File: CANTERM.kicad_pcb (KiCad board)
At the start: 2 copper layers, 25.4 x 50.8 mm, 10 parts, among them J1 Conn_01x03_Pin, J2 Conn_01x03_Pin, J3 Conn_01x03_Pin, M1 MountingHole_10, M2 MountingHole_10, SW1 SW_DIP_x01

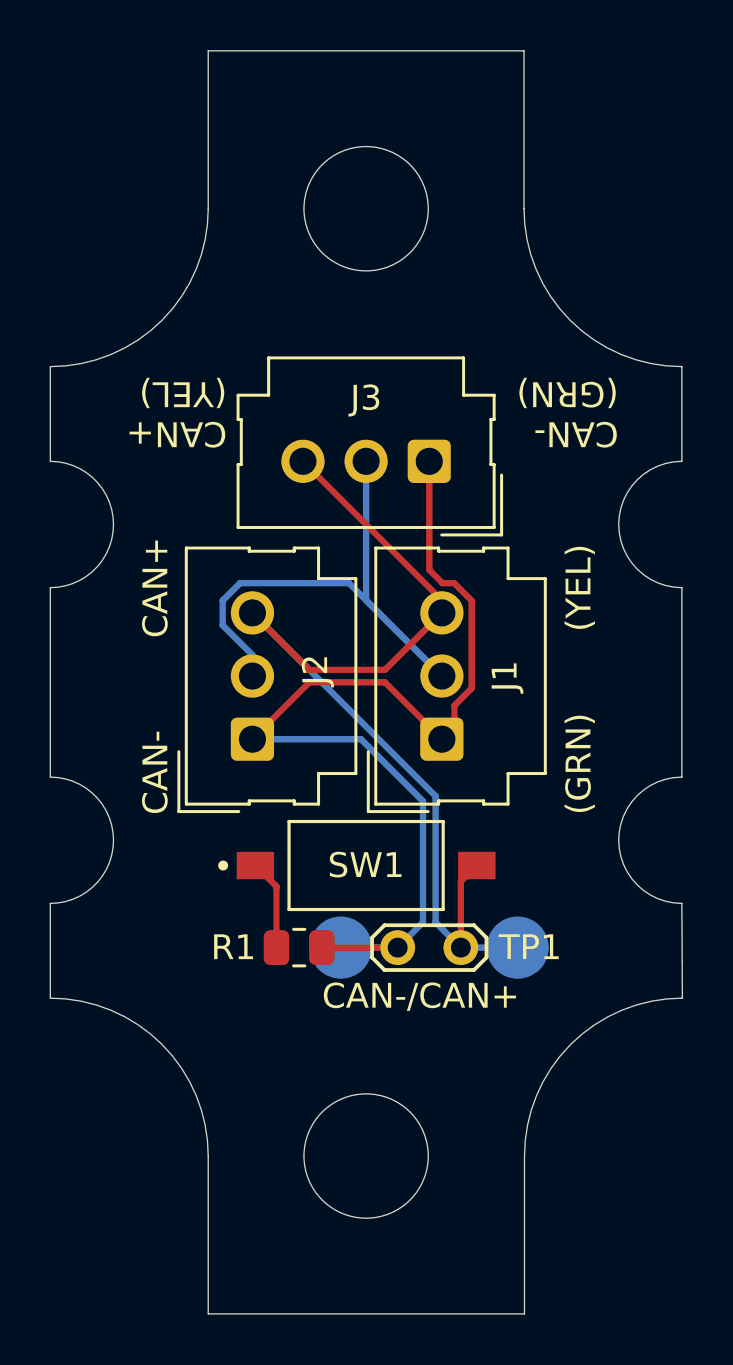
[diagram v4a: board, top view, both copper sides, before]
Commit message: slightly shrink board so it fits _inside_ the space envelope
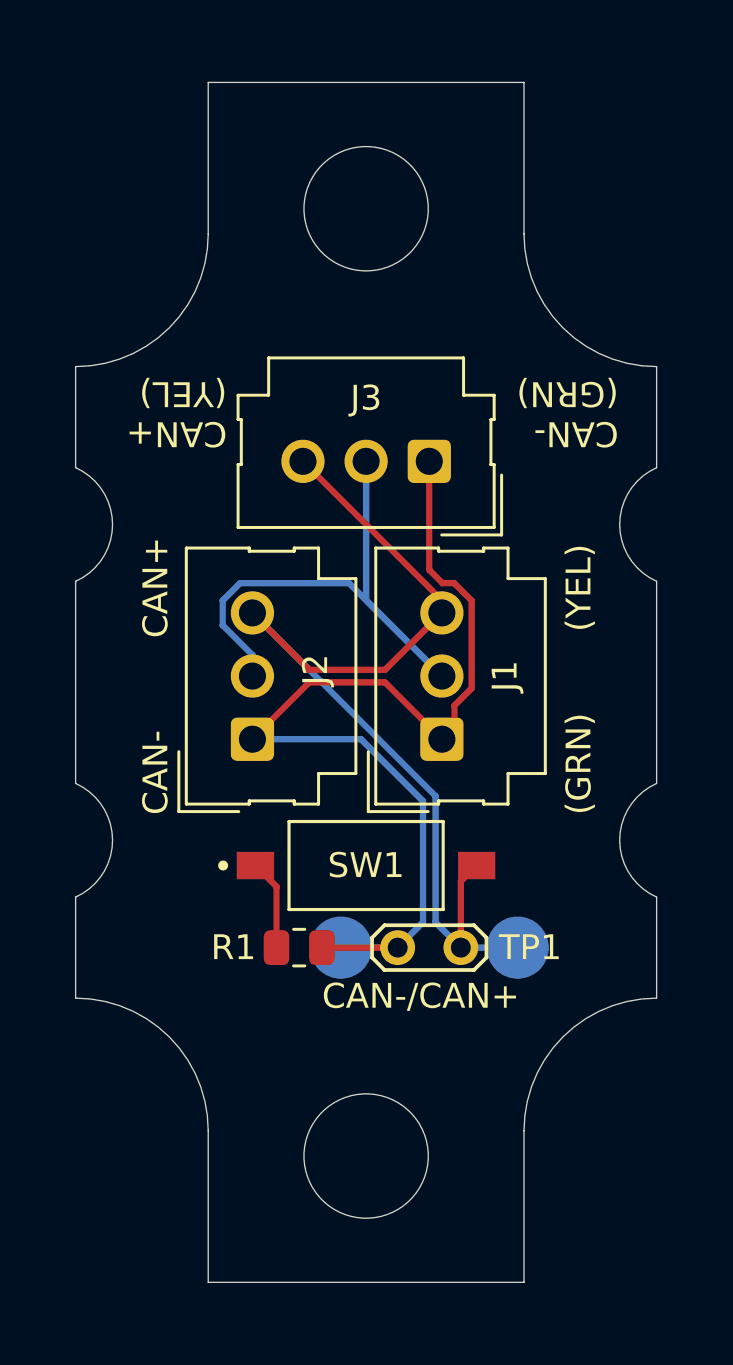
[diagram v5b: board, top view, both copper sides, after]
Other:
- board size 25.4 x 50.8 mm -> 23.4 x 48.3 mm
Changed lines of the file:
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@@
 		)
 	)
-	(gr_line
-		(start 100 60.16)
-		(end 100 56.35)
+	(gr_arc
+		(start 101.016 73.114001)
+		(mid 102.501609 75.4)
+		(end 101.016 77.685999)
 		(stroke
 			(width 0.05)
@@
 	)
 	(gr_arc
-		(start 100 72.86)
-		(mid 102.54 75.4)
-		(end 100 77.94)
-		(locked yes)
+		(start 106.35 51.016)
+		(mid 104.787708 54.787708)
+		(end 101.016 56.35)
 		(stroke
 			(width 0.05)
@@
 	)
 	(gr_line
-		(start 106.35 43.65)
-		(end 106.35 50)
+		(start 124.384 77.686)
+		(end 124.384 81.75)
 		(stroke
 			(width 0.05)
@@
 	)
 	(gr_line
-		(start 125.4 65.24)
-		(end 125.4 72.86)
-		(locked yes)
+		(start 124.384 56.35)
+		(end 124.384 60.414)
+		(stroke
+			(width 0.05)
+			(type default)
+		)
+		(layer "Edge.Cuts")
+	)
+	(gr_line
+		(start 101.016 60.414)
+		(end 101.016 56.35)
 		(stroke
 			(width 0.05)
@@
 	)
 	(gr_arc
-		(start 100 60.16)
-		(mid 102.54 62.7)
-		(end 100 65.24)
-		(locked yes)
+		(start 119.05 87.084)
+		(mid 120.612292 83.312292)
+		(end 124.384 81.75)
 		(stroke
 			(width 0.05)
@@
 	)
 	(gr_arc
-		(start 125.4 56.35)
-		(mid 120.909872 54.490128)
-		(end 119.05 50)
+		(start 124.384 64.985999)
+		(mid 122.898391 62.7)
+		(end 124.384 60.414001)
 		(stroke
 			(width 0.05)
@@
 	)
 	(gr_line
-		(start 125.4 56.35)
-		(end 125.4 60.16)
+		(start 106.35 93.18)
+		(end 119.05 93.18)
+		(stroke
+			(width 0.05)
+			(type default)
+		)
+		(layer "Edge.Cuts")
+	)
+	(gr_line
+		(start 106.35 44.92)
+		(end 106.35 51.016)
+		(stroke
+			(width 0.05)
+			(type default)
+		)
+		(layer "Edge.Cuts")
+	)
+	(gr_line
+		(start 119.05 93.18)
+		(end 119.05 87.084)
 		(stroke
 			(width 0.05)
@@
 	)
 	(gr_arc
-		(start 106.35 50)
-		(mid 104.490128 54.490128)
-		(end 100 56.35)
+		(start 101.016 60.414)
+		(mid 102.501609 62.699999)
+		(end 101.016 64.985998)
 		(stroke
 			(width 0.05)
@@
 	)
 	(gr_arc
-		(start 125.4 77.94)
-		(mid 122.86 75.4)
-		(end 125.4 72.86)
-		(locked yes)
+		(start 101.016 81.75)
+		(mid 104.787708 83.312292)
+		(end 106.35 87.084)
 		(stroke
 			(width 0.05)
@@
 	)
 	(gr_line
-		(start 100 72.86)
-		(end 100 65.24)
-		(locked yes)
+		(start 101.016 73.114)
+		(end 101.016 64.986)
 		(stroke
 			(width 0.05)
@@
 	)
 	(gr_line
-		(start 125.42 81.75)
-		(end 125.4 77.94)
+		(start 101.016 81.75)
+		(end 101.016 77.686)
 		(stroke
 			(width 0.05)
@@
 	)
 	(gr_line
-		(start 100 81.75)
-		(end 100 77.94)
+		(start 106.35 87.084)
+		(end 106.35 93.18)
+		(stroke
+			(width 0.05)
+			(type default)
+		)
+		(layer "Edge.Cuts")
+	)
+	(gr_arc
+		(start 124.384 77.686)
+		(mid 122.898391 75.400001)
+		(end 124.384 73.114002)
 		(stroke
 			(width 0.05)
@@
 	)
 	(gr_line
-		(start 106.35 94.45)
-		(end 106.35 88.1)
+		(start 119.05 44.92)
+		(end 106.35 44.92)
+		(stroke
+			(width 0.05)
+			(type default)
+		)
+		(layer "Edge.Cuts")
+	)
+	(gr_arc
+		(start 124.384 56.35)
+		(mid 120.612292 54.787708)
+		(end 119.05 51.016)
 		(stroke
 			(width 0.05)
@@
 	)
 	(gr_line
-		(start 119.05 43.65)
-		(end 106.35 43.65)
+		(start 119.05 51.016)
+		(end 119.05 44.92)
 		(stroke
 			(width 0.05)
@@
 	)
 	(gr_line
-		(start 119.07 88.1)
-		(end 119.07 94.45)
+		(start 124.384 64.986)
+		(end 124.384 73.114)
 		(stroke
 			(width 0.05)
-			(type default)
-		)
-		(layer "Edge.Cuts")
-	)
-	(gr_arc
-		(start 100 81.75)
-		(mid 104.490128 83.609872)
-		(end 106.35 88.1)
-		(stroke
-			(width 0.05)
-			(type default)
-		)
-		(layer "Edge.Cuts")
-	)
-	(gr_line
-		(start 119.07 94.45)
-		(end 106.35 94.45)
-		(stroke
-			(width 0.05)
-			(type default)
-		)
-		(layer "Edge.Cuts")
-	)
-	(gr_line
-		(start 119.05 50)
-		(end 119.05 43.65)
-		(stroke
-			(width 0.05)
-			(type default)
-		)
-		(layer "Edge.Cuts")
-	)
-	(gr_arc
-		(start 125.4 65.24)
-		(mid 122.86 62.7)
-		(end 125.4 60.16)
-		(locked yes)
-		(stroke
-			(width 0.05)
-			(type default)
-		)
-		(layer "Edge.Cuts")
-	)
-	(gr_arc
-		(start 119.07 88.1)
-		(mid 120.929872 83.609872)
-		(end 125.42 81.75)
-		(stroke
-			(width 0.05)

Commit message: crying, correctly labeled pins
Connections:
- J1 pad 1: CAN- -> CAN+
- J1 pad 3: CAN+ -> CAN-
- J2 pad 1: CAN- -> CAN+
- J2 pad 3: CAN+ -> CAN-
- J3 pad 1: CAN- -> CAN+
- J3 pad 3: CAN+ -> CAN-
- R1 pad 1: CAN- -> CAN+
- SW1 pad 2: CAN+ -> CAN-
- TP1 pad 1: CAN- -> CAN+
- TP1 pad 2: CAN+ -> CAN-
- TP2 pad 1: CAN+ -> CAN-
- TP3 pad 1: CAN- -> CAN+
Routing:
- net CAN-: track 41.7 -> 40.7 mm
- net CAN+: track 40.7 -> 41.7 mm
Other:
- board text added: "WM CAN Term/Conn Rev 3"
- board text removed: "CAN-/CAN+"
- board text removed: "WM CAN Term/Conn Rev 2"
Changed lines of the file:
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@@
 			(remove_unused_layers no)
 			(roundrect_rratio 0.143678)
-			(net 2 "CAN-")
+			(net 1 "CAN+")
 			(pinfunction "Pin_1")
 			(pintype "passive")
@@
 			(layers "*.Cu" "*.Mask")
 			(remove_unused_layers no)
-			(net 1 "CAN+")
+			(net 2 "CAN-")
 			(pinfunction "Pin_3")
 			(pintype "passive")
@@
 			(remove_unused_layers no)
 			(roundrect_rratio 0.143678)
-			(net 2 "CAN-")
+			(net 1 "CAN+")
 			(pinfunction "Pin_1")
 			(pintype "passive")
@@
 			(layers "*.Cu" "*.Mask")
 			(remove_unused_layers no)
-			(net 1 "CAN+")
+			(net 2 "CAN-")
 			(pinfunction "Pin_3")
 			(pintype "passive")
@@
 			(remove_unused_layers no)
 			(roundrect_rratio 0.143678)
-			(net 2 "CAN-")
+			(net 1 "CAN+")
 			(pinfunction "Pin_1")
 			(pintype "passive")
@@
 			(layers "*.Cu" "*.Mask")
 			(remove_unused_layers no)
-			(net 1 "CAN+")
+			(net 2 "CAN-")
 			(pinfunction "Pin_3")
 			(pintype "passive")
@@
 			(layers "F.Cu" "F.Paste" "F.Mask")
 			(roundrect_rratio 0.243902)
-			(net 2 "CAN-")
+			(net 1 "CAN+")
 			(pintype "passive")
 		)
@@
 			(size 1.5 1.1)
 			(layers "F.Cu" "F.Paste" "F.Mask")
-			(net 1 "CAN+")
+			(net 2 "CAN-")
 			(pintype "passive")
 			(solder_mask_margin 0.102)
@@
 			(layers "*.Cu" "*.Mask")
 			(remove_unused_layers no)
-			(net 2 "CAN-")
+			(net 1 "CAN+")
 			(pinfunction "1")
 			(pintype "passive")
@@
 			(layers "*.Cu" "*.Mask")
 			(remove_unused_layers no)
-			(net 1 "CAN+")
+			(net 2 "CAN-")
 			(pinfunction "2")
 			(pintype "passive")
@@
 			(size 2.5 2.5)
 			(layers "B.Cu" "B.Mask")
-			(net 2 "CAN-")
+			(net 1 "CAN+")
 			(pinfunction "1")
 			(pintype "passive")
@@
 			(size 2.5 2.5)
 			(layers "B.Cu" "B.Mask")
-			(net 1 "CAN+")
+			(net 2 "CAN-")
 			(pinfunction "1")
 			(pintype "passive")
@@
 		(layer "User.9")
 	)
-	(gr_text "WM CAN Term/Conn\nRev 2"
+	(gr_text "WM CAN Term/Conn\nRev 3"
 		(at 106.35 56.604 90)
 		(layer "B.SilkS")
@@
 		)
 	)
-	(gr_text "CAN-\n(GRN)"
+	(gr_text "CAN+\n(YEL)"
 		(at 122.86 56.858 180)
 		(layer "F.SilkS")
@@
 		)
 	)
-	(gr_text "CAN+"
+	(gr_text "CAN-"
 		(at 104.826 67.272 90)
 		(layer "F.SilkS")
@@
 		)
 	)
-	(gr_text "(YEL)"
-		(at 121.844 67.018 90)
+	(gr_text "(GRN)"
+		(at 121.844 67.526 90)
 		(layer "F.SilkS")
 		(effects
@@
 		)
 	)
-	(gr_text "(GRN)"
+	(gr_text "(YEL)"
 		(at 121.844 74.384 90)
 		(layer "F.SilkS")
@@
 		)
 	)
-	(gr_text "CAN-/CAN+"
+	(gr_text "CAN+/CAN-"
 		(at 110.922 82.258 0)
 		(layer "F.SilkS")
@@
 		)
 	)
-	(gr_text "CAN+\n(YEL)"
-		(at 107.112 56.858 180)
+	(gr_text "CAN-\n(GRN)"
+		(at 106.858 56.858 180)
 		(layer "F.SilkS")
 		(effects
@@
 		)
 	)
-	(gr_text "CAN-"
+	(gr_text "CAN+"
 		(at 104.826 74.384 90)
 		(layer "F.SilkS")
@@
 	)
 	(segment
+		(start 113.46 69.048)
+		(end 110.416 69.048)
+		(width 0.254)
+		(layer "F.Cu")
+		(net 1)
+	)
+	(segment
+		(start 115.24 60.16)
+		(end 115.24 64.527236)
+		(width 0.254)
+		(layer "F.Cu")
+		(net 1)
+	)
+	(segment
+		(start 116.252 69.984814)
+		(end 116.252 70.832)
+		(width 0.254)
+		(layer "F.Cu")
+		(net 1)
+	)
+	(segment
+		(start 115.748 71.336)
+		(end 113.46 69.048)
+		(width 0.254)
+		(layer "F.Cu")
+		(net 1)
+	)
+	(segment
+		(start 116.252 70.832)
+		(end 115.748 71.336)
+		(width 0.254)
+		(layer "F.Cu")
+		(net 1)
+	)
+	(segment
+		(start 116.945 65.760186)
+		(end 116.945 69.291814)
+		(width 0.254)
+		(layer "F.Cu")
+		(net 1)
+	)
+	(segment
+		(start 115.24 64.527236)
+		(end 115.771764 65.059)
+		(width 0.254)
+		(layer "F.Cu")
+		(net 1)
+	)
+	(segment
+		(start 115.771764 65.059)
+		(end 116.243814 65.059)
+		(width 0.254)
+		(layer "F.Cu")
+		(net 1)
+	)
+	(segment
+		(start 110.416 69.048)
+		(end 108.128 71.336)
+		(width 0.254)
+		(layer "F.Cu")
+		(net 1)
+	)
+	(segment
+		(start 113.97 79.718)
+		(end 110.922 79.718)
+		(width 0.254)
+		(layer "F.Cu")
+		(net 1)
+	)
+	(segment
+		(start 116.945 69.291814)
+		(end 116.252 69.984814)
+		(width 0.254)
+		(layer "F.Cu")
+		(net 1)
+	)
+	(segment
+		(start 116.243814 65.059)
+		(end 116.945 65.760186)
+		(width 0.254)
+		(layer "F.Cu")
+		(net 1)
+	)
+	(segment
+		(start 114.988 73.828764)
+		(end 112.495236 71.336)
+		(width 0.254)
+		(layer "B.Cu")
+		(net 1)
+	)
+	(segment
+		(start 112.495236 71.336)
+		(end 108.128 71.336)
+		(width 0.254)
+		(layer "B.Cu")
+		(net 1)
+	)
+	(segment
+		(start 113.97 79.718)
+		(end 114.988 78.7)
+		(width 0.254)
+		(layer "B.Cu")
+		(net 1)
+	)
+	(segment
+		(start 114.988 78.7)
+		(end 114.988 73.828764)
+		(width 0.254)
+		(layer "B.Cu")
+		(net 1)
+	)
+	(segment
+		(start 113.97 79.718)
+		(end 111.684 79.718)
+		(width 0.254)
+		(layer "B.Cu")
+		(net 1)
+	)
+	(segment
 		(start 110.16 60.16)
 		(end 115.748 65.748)
 		(width 0.254)
 		(layer "F.Cu")
-		(net 1)
+		(net 2)
 	)
 	(segment
@@
 		(width 0.254)
 		(layer "F.Cu")
-		(net 1)
+		(net 2)
 	)
 	(segment
@@
 		(width 0.254)
 		(layer "F.Cu")
-		(net 1)
+		(net 2)
 	)
 	(segment
@@
 		(width 0.254)
 		(layer "F.Cu")
-		(net 1)
+		(net 2)
 	)
 	(segment
@@
 		(width 0.254)
 		(layer "F.Cu")
-		(net 1)
+		(net 2)
 	)
 	(segment
@@
 		(width 0.254)
 		(layer "F.Cu")
-		(net 1)
+		(net 2)
 	)
 	(segment
@@
 		(width 0.254)
 		(layer "F.Cu")
-		(net 1)
+		(net 2)
 	)
 	(segment
@@
 		(width 0.254)
 		(layer "B.Cu")
-		(net 1)
+		(net 2)
 	)
 	(segment
@@
 		(width 0.254)
 		(layer "B.Cu")
-		(net 1)
+		(net 2)
 	)
 	(segment
@@
 		(width 0.254)
 		(layer "B.Cu")
-		(net 1)
+		(net 2)
 	)
 	(segment
@@
 		(width 0.254)
 		(layer "B.Cu")
-		(net 1)
-	)
-	(segment
-		(start 113.46 69.048)
-		(end 110.416 69.048)
-		(width 0.254)
-		(layer "F.Cu")
-		(net 2)
-	)
-	(segment
-		(start 115.24 60.16)
-		(end 115.24 64.527236)
-		(width 0.254)
-		(layer "F.Cu")
-		(net 2)
-	)
-	(segment
-		(start 116.252 69.984814)
-		(end 116.252 70.832)
-		(width 0.254)
-		(layer "F.Cu")
-		(net 2)
-	)
-	(segment
-		(start 115.748 71.336)
-		(end 113.46 69.048)
-		(width 0.254)
-		(layer "F.Cu")
-		(net 2)
-	)
-	(segment
-		(start 116.252 70.832)
-		(end 115.748 71.336)
-		(width 0.254)
-		(layer "F.Cu")
-		(net 2)
-	)
-	(segment
-		(start 116.945 65.760186)
-		(end 116.945 69.291814)
-		(width 0.254)
-		(layer "F.Cu")
-		(net 2)
-	)
-	(segment
-		(start 115.24 64.527236)
-		(end 115.771764 65.059)
-		(width 0.254)
-		(layer "F.Cu")
-		(net 2)
-	)
-	(segment
-		(start 115.771764 65.059)
-		(end 116.243814 65.059)
-		(width 0.254)
-		(layer "F.Cu")
-		(net 2)
-	)
-	(segment
-		(start 110.416 69.048)
-		(end 108.128 71.336)
-		(width 0.254)
-		(layer "F.Cu")
-		(net 2)
-	)
-	(segment
-		(start 113.97 79.718)
-		(end 110.922 79.718)
-		(width 0.254)
-		(layer "F.Cu")
-		(net 2)
-	)
-	(segment
-		(start 116.945 69.291814)
-		(end 116.252 69.984814)
-		(width 0.254)
-		(layer "F.Cu")
-		(net 2)
-	)
-	(segment
-		(start 116.243814 65.059)
-		(end 116.945 65.760186)
-		(width 0.254)
-		(layer "F.Cu")
-		(net 2)
-	)
-	(segment
-		(start 114.988 73.828764)
-		(end 112.495236 71.336)
-		(width 0.254)
-		(layer "B.Cu")
-		(net 2)
-	)
-	(segment
-		(start 112.495236 71.336)
-		(end 108.128 71.336)
-		(width 0.254)
-		(layer "B.Cu")
-		(net 2)
-	)
-	(segment
-		(start 113.97 79.718)
-		(end 114.988 78.7)
-		(width 0.254)
-		(layer "B.Cu")
-		(net 2)
-	)
-	(segment
-		(start 114.988 78.7)
-		(end 114.988 73.828764)
-		(width 0.254)
-		(layer "B.Cu")
-		(net 2)
-	)
-	(segment
-		(start 113.97 79.718)
-		(end 111.684 79.718)
-		(width 0.254)
-		(layer "B.Cu")
